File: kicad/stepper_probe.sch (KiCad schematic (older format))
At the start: 55 parts, among them J1 Conn_01x04_Male, J2 Conn_01x04_Male, J3 BAT, J4 Serial Port, J5 SWD, J6 BAT, J7 Conn_01x01_Female, J8 Conn_01x01_Female, M1 Motor, SW1 SW_Push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

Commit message: Work in progress.
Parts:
- removed R1, R2, R3, R4: 10R, stepper_probe:R_0402_1005Metric_Pad0.72x0.64mm_HandSolder, symbol Device:R_Small_US
- added F1, F2, F3, F4: 500ma, stepper_probe:Fuse_0402, symbol Device:Fuse_Small
- R13: value 0R -> 5R; LCSC C17168 -> ????
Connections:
- net STEPPER1: now also F1.1
- net STEPPER2: now also F2.1
- net STEPPER3: now also F3.1
- net STEPPER4: now also F4.1
- net at D4.4 (~~): now also F4.2
- net at C7.1, C8.1, D6.1 (K): now also R13.1, U4.1 (IN); no longer D4.1 (+), D5.1 (+), R13.2
- net at D4.3 (~~): now also F3.2
- net at D5.3 (~~): now also F1.2
- net at D5.4 (~~): now also F2.2
- new net: D4.1 (+), D5.1 (+), R13.2
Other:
- moved on the sheet: C10, C11, C9, D4, D5, R13, R14, U4

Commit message: Minor clean ups.
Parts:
- removed D4, D5: MB1S, stepper_probe:DIODE_BRIDGE, symbol stepper_probe:DIODE_BRIDGE
- removed D6: 1N5819WS, stepper_probe:D_SOD-323_HandSoldering, symbol Device:D_Schottky
- removed F1, F2, F3, F4: 500ma, stepper_probe:Fuse_0402, symbol Device:Fuse_Small
- removed J7: Conn_01x01_Female, stepper_probe:BAT_PLUS_PAD, symbol Connector:Conn_01x01_Female
- removed J8: Conn_01x01_Female, stepper_probe:BAT_MINUS_PAD, symbol Connector:Conn_01x01_Female
- removed R13: 5R, stepper_probe:R_0402_1005Metric_Pad0.72x0.64mm_HandSolder, symbol Device:R_Small_US
- added Q1: PJA3439, Package_TO_SOT_SMD:SOT-23, symbol stepper_probe:P_MOSFET
- added R1: 300k, stepper_probe:R_0402_1005Metric_Pad0.72x0.64mm_HandSolder, symbol Device:R_Small_US
- J3: footprint stepper_probe:PinHeader_1x02_P2.54mm_Vertical -> stepper_probe:connector_2pins_horizontal; LCSC (none) -> C30436
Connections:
- net GND: now also Q1.1 (G), R1.1
- net at C7.1, C8.1, U4.1 (IN): now also Q1.2 (S)
- net BAT+: no longer names the net of J3.2 (Pin_2)
- net BAT+: now also Q1.3 (D), R1.2
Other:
- note added: "-"
- note added: "VIN\n5-30VDC"
- note removed: "9V battery pads for zero \ncurrent calibration."
- note removed: "OPTIONAL BAT"
- moved on the sheet: C10, C11, C12, C7, C8, C9, J3, J4, J5, R10, R14, R8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

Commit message: Cleaned up power in header.
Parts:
- J3: footprint stepper_probe:connector_2pins_horizontal -> stepper_probe:PinHeader_1x02_P2.54mm_Vertical_JLCPCB_SMD; LCSC C30436 -> C2905434
- J4: LCSC (none) -> DNP
- J6: value BAT -> Reset header; LCSC (none) -> DNP
- Q1: footprint Package_TO_SOT_SMD:SOT-23 -> stepper_probe:SOT-23_JLCPCB
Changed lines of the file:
@@
 F 0 "J3" H 5875 1500 50  0000 R CNN
 F 1 "BAT" H 5625 1675 50  0001 R CNN
-F 2 "stepper_probe:connector_2pins_horizontal" H 5775 1725 50  0001 C CNN
+F 2 "stepper_probe:PinHeader_1x02_P2.54mm_Vertical_JLCPCB_SMD" H 5775 1725 50  0001 C CNN
 F 3 "~" H 5775 1725 50  0001 C CNN
-F 4 "C30436" H 5775 1725 50  0001 C CNN "LCSC"
+F 4 "C2905434" H 5775 1725 50  0001 C CNN "LCSC"
 	1    5775 1725
 	1    0    0    1
@@
 F 2 "stepper_probe:PinHeader_1x04_P2.54mm_Vertical" H 10075 3600 50  0001 C CNN
 F 3 "~" H 10075 3600 50  0001 C CNN
-F 4 "" H 10075 3600 50  0001 C CNN "LCSC"
+F 4 "DNP" H 10075 3600 50  0001 C CNN "LCSC"
 	1    10075 3600
 	-1   0    0    -1
@@
 P 5250 4625
 F 0 "J6" H 5350 4425 50  0000 R CNN
-F 1 "BAT" H 5100 4575 50  0001 R CNN
+F 1 "Reset header" H 5100 4575 50  0001 R CNN
 F 2 "stepper_probe:PinHeader_1x02_P2.54mm_Vertical" H 5250 4625 50  0001 C CNN
 F 3 "~" H 5250 4625 50  0001 C CNN
-F 4 "" H 5250 4625 50  0001 C CNN "LCSC"
+F 4 "DNP" H 5250 4625 50  0001 C CNN "LCSC"
 	1    5250 4625
 	-1   0    0    -1
@@
 F 0 "Q1" V 7065 1725 50  0000 C CNN
 F 1 "PJA3439" V 6974 1725 50  0000 C CNN
-F 2 "Package_TO_SOT_SMD:SOT-23" H 6850 1650 50  0001 L CIN
+F 2 "stepper_probe:SOT-23_JLCPCB" H 6850 1650 50  0001 L CIN
 F 3 "http://www.aosmd.com/pdfs/datasheet/AO3401A.pdf" H 6650 1725 50  0001 L CNN
 F 4 "C2844879" V 6883 1725 50  0000 C CNN "LCSC"

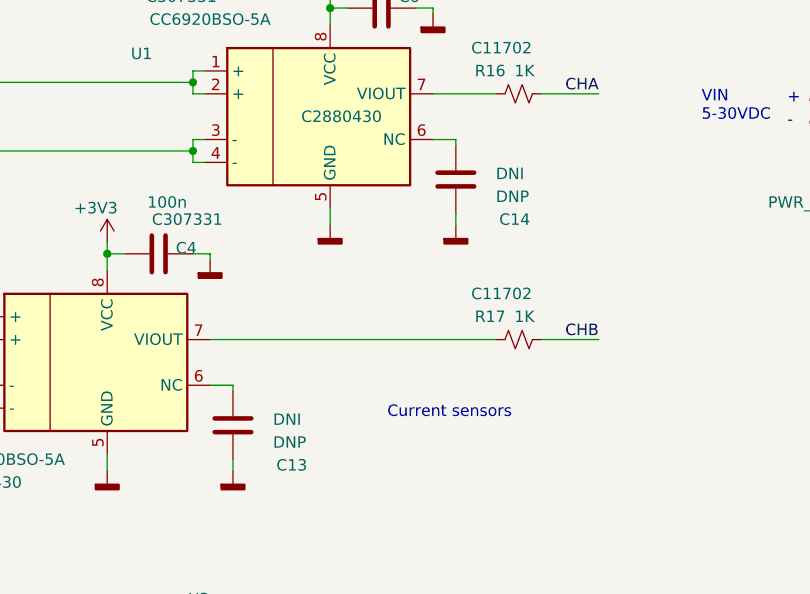
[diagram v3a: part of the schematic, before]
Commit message: Minor change of 'DNI' to 'DNP' for consistency.
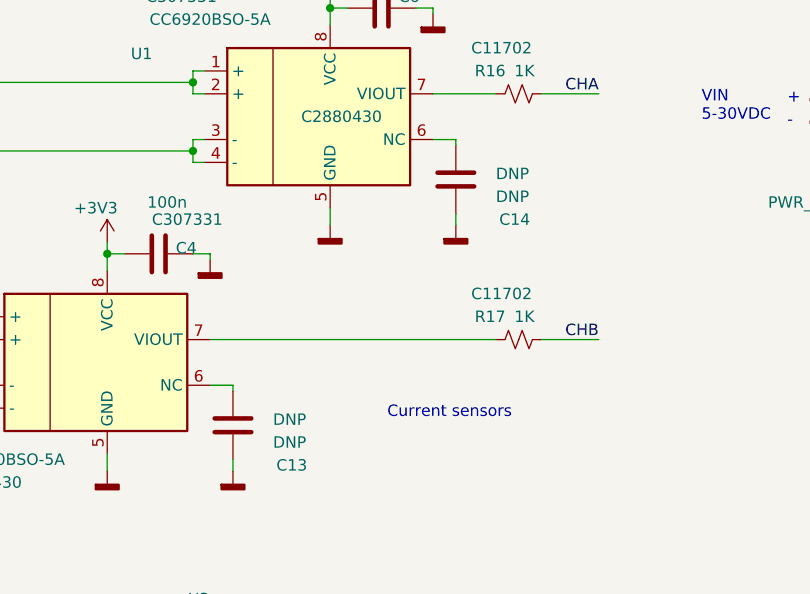
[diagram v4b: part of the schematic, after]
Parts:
- C13, C14: value DNI -> DNP
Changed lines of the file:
@@
 P 3250 3050
 F 0 "C13" H 2925 3225 50  0000 L CNN
-F 1 "DNI" H 3075 3025 50  0000 R CNN
+F 1 "DNP" H 3075 3025 50  0000 R CNN
 F 2 "stepper_probe:C_0402_1005Metric_Pad0.74x0.62mm_HandSolder" H 3288 2900 50  0001 C CNN
 F 3 "~" H 3250 3050 50  0001 C CNN
@@
 P 4225 1975
 F 0 "C14" H 3900 2150 50  0000 L CNN
-F 1 "DNI" H 4050 1950 50  0000 R CNN
+F 1 "DNP" H 4050 1950 50  0000 R CNN
 F 2 "stepper_probe:C_0402_1005Metric_Pad0.74x0.62mm_HandSolder" H 4263 1825 50  0001 C CNN
 F 3 "~" H 4225 1975 50  0001 C CNN

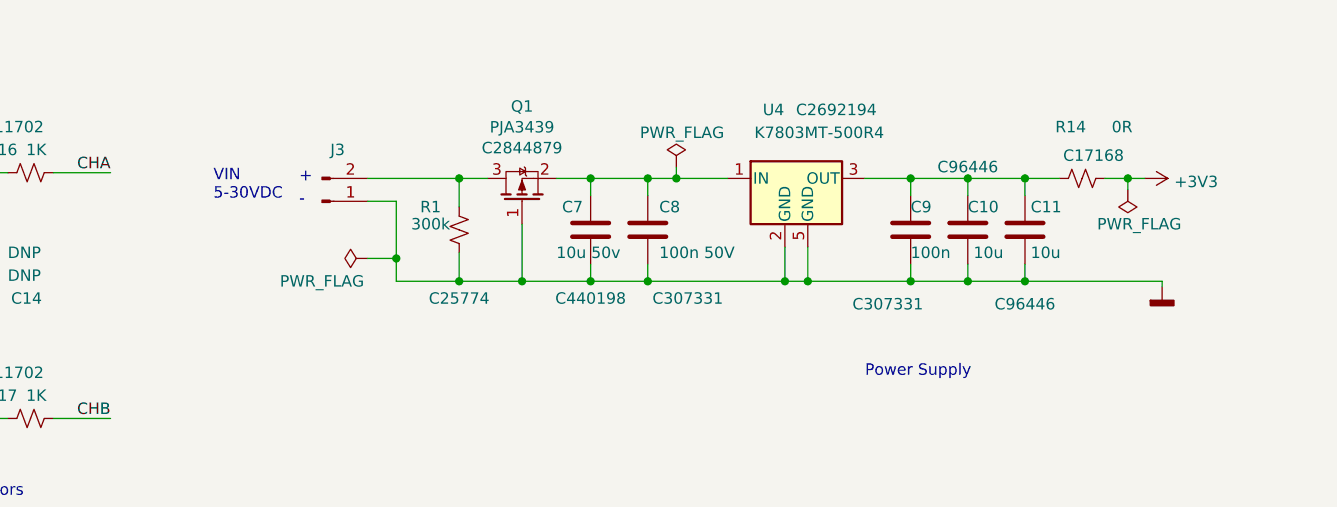
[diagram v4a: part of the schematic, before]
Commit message: Added zener protection
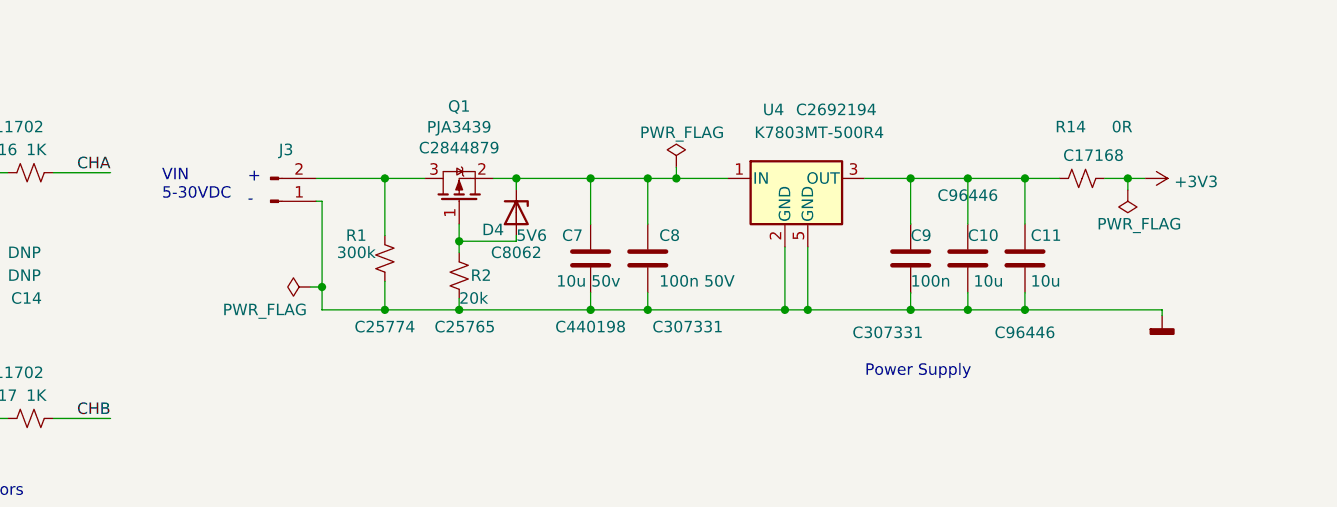
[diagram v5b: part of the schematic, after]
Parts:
- added D4: 5V6, Diode_SMD:D_MiniMELF, symbol stepper_probe:zenner
- added R2: 20k, stepper_probe:R_0402_1005Metric_Pad0.72x0.64mm_HandSolder, symbol Device:R_Small_US
- J3: footprint stepper_probe:PinHeader_1x02_P2.54mm_Vertical_JLCPCB_SMD -> stepper_probe:PinHeader_1x02_P2.54mm_Horizontal_JLCPCB; LCSC C2905434 -> C2935927
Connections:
- net GND: now also R2.1; no longer Q1.1 (G)
- net at C7.1, C8.1, Q1.2 (S)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: now also D4.1 (K)
- new net: D4.2 (A), Q1.1 (G), R2.2
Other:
- moved on the sheet: C10, C11, C7, C8, C9, J3, Q1, R1
